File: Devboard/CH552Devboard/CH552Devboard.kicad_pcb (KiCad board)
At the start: 2 copper layers, 25.6 x 24.6 mm, 14 parts, among them J1 D+, J2 USB_B_Micro, J3 System, J4 GPIO, SW1 SW_Push, SW2 SW_Push, SW3 SW_Push, SW4 SW_Push, U1 CH552T

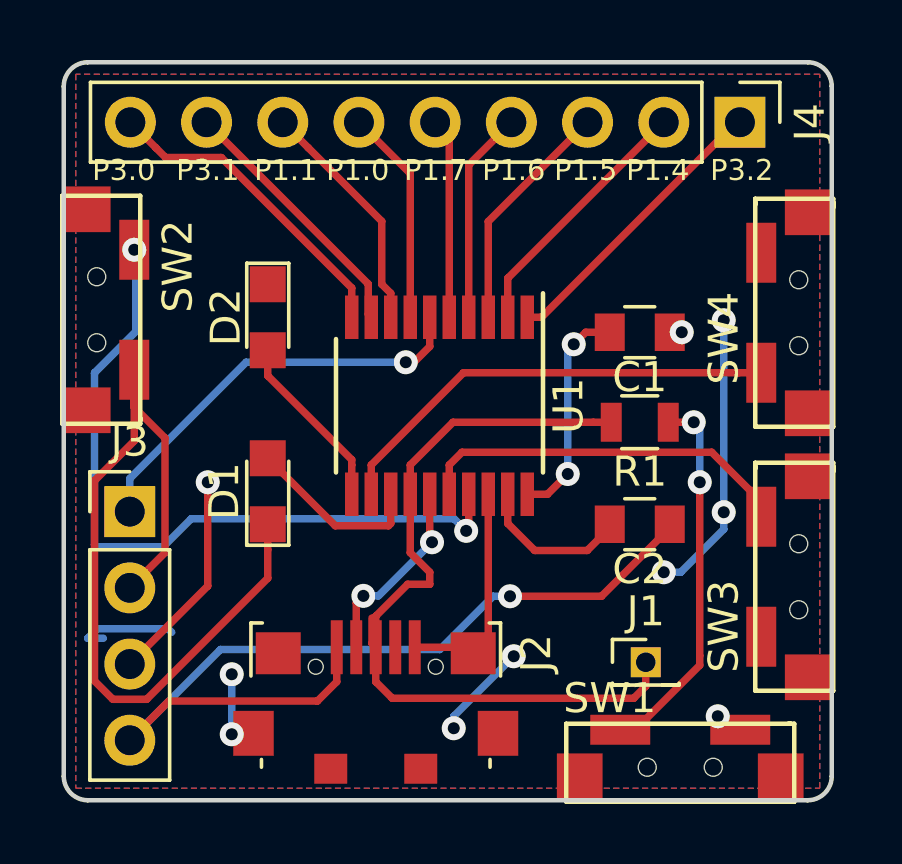
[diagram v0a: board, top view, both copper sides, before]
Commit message: Recieved V1, fixed issue. Seems to work now.
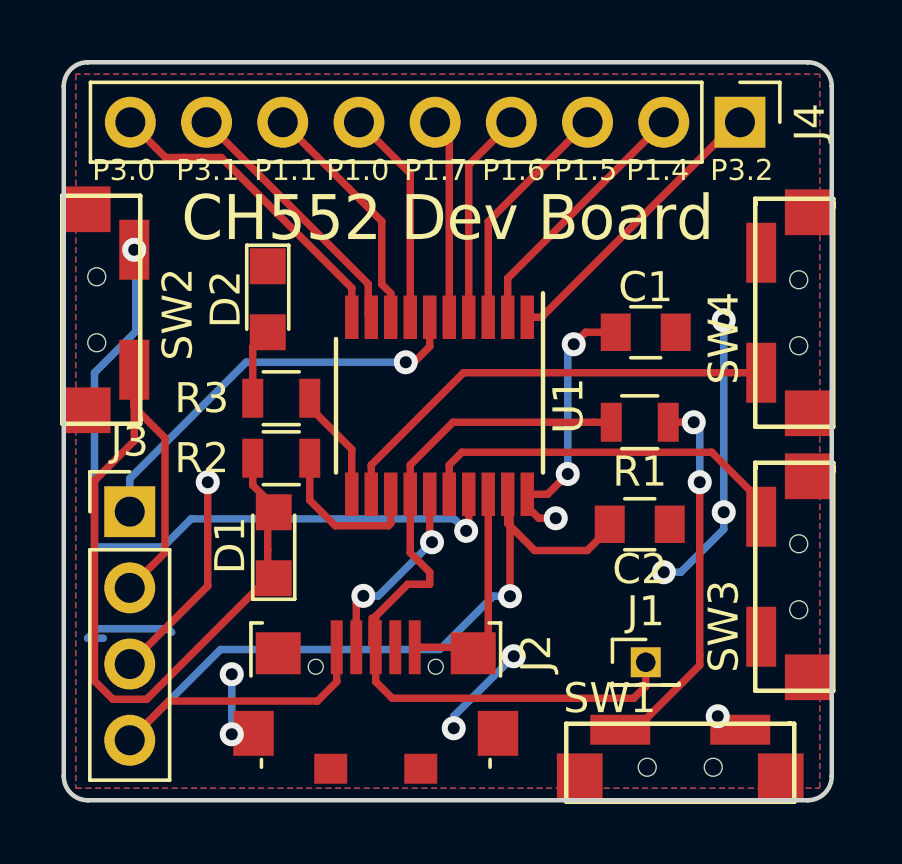
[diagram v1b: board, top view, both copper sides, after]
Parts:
- added R2: 330ohm, Resistors_SMD:R_0805, F.Cu at (163.2, 111.2)
- added R3: 330ohm, Resistors_SMD:R_0805, F.Cu at (163.2, 109.2)
- C1, C2: value C_Small -> 0.1uF
- moved D1 1.81 mm to (163.0, 114.1)
- moved D2 0.60 mm to (162.8, 105.9)
- moved C1 0.20 mm to (175.4, 107.0), turned to 0 degrees
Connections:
- C1 pad 2: Net-(C1-Pad2) -> VSS
- C2 pad 1: VCC -> VSS
- C2 pad 2: Net-(C2-Pad2) -> VCC
- U1 pad 11: Net-(D2-Pad2) -> Net-(R3-Pad2)
- U1 pad 13: Net-(D1-Pad2) -> Net-(R2-Pad2)
- U1 pad 19: Net-(C2-Pad2) -> VCC
- U1 pad 20: Net-(C1-Pad2) -> +3V3
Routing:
- net +3V3: track 7.14 -> 15.6 mm, vias 3 -> 5
- net Net-(C1-Pad2): track 7.40 -> 0.00 mm, vias 2 -> 0
- net Net-(R2-Pad2): track 0.00 -> 5.46 mm
- net Net-(C2-Pad2): track 5.18 -> 0.00 mm
- net Net-(D1-Pad2): track 6.04 -> 2.08 mm
- net Net-(R3-Pad2): track 0.00 -> 3.78 mm
- net Net-(D2-Pad2): track 5.96 -> 2.41 mm
- net VCC: track 29.9 -> 32.1 mm
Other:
- board text added: "CH552 Dev Board"
- board text added: "V2"

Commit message: Added silkscreen to devboard
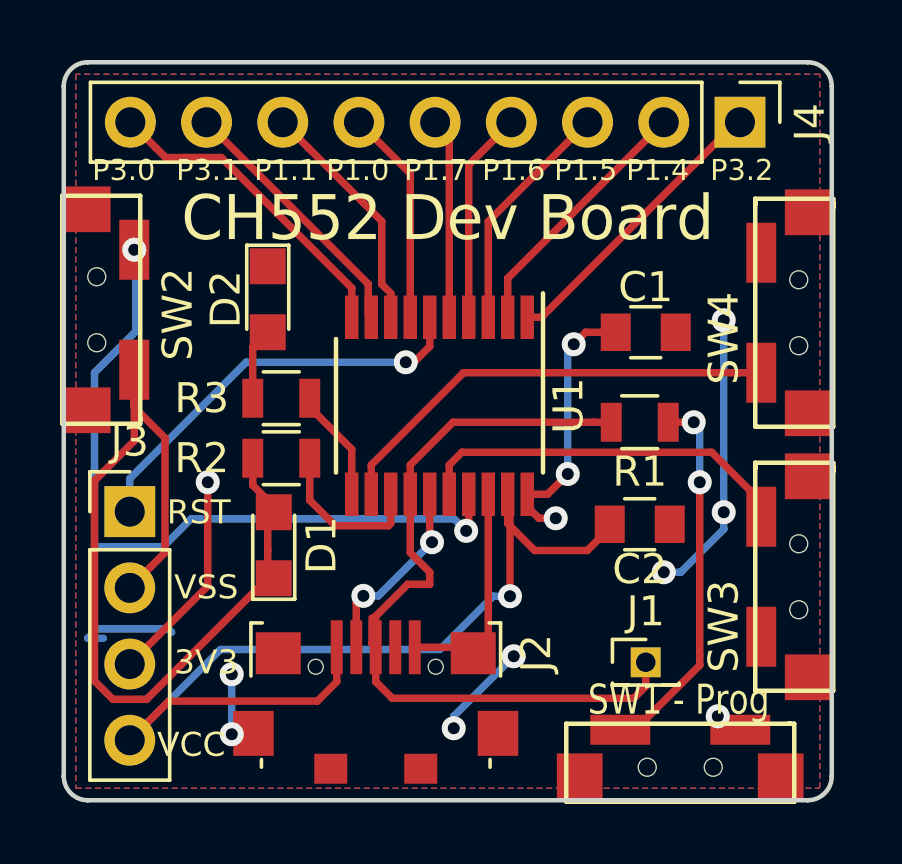
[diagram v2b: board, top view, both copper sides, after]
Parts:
- SW1 - Prog: renamed from SW1
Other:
- board text added: "3V3"
- board text added: "D1: P3.5 D2: P3.3 SW2: P1.2 SW3: P1.3 SW4: P3.4"
- board text added: "RST"
- board text added: "To Program: Reset uC while holding SW1 (Prog)"
- board text added: "VCC"
- board text added: "VSS"
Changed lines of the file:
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@@
   (general
     (thickness 1.6)
-    (drawings 19)
+    (drawings 25)
     (tracks 172)
     (zones 0)
@@
     (tags "LED led 0805 SMD smd SMT smt smdled SMDLED smtled SMTLED")
     (attr smd)
-    (fp_text reference D1 (at 0 -1.45 90) (layer F.SilkS)
+    (fp_text reference D1 (at 0 1.592 90) (layer F.SilkS)
       (effects (font (size 1 1) (thickness 0.15)))
     )
@@
   (module CH552:Ali_button (layer F.Cu)
     (at 176.7 121.65)
-    (fp_text reference SW1 (at -2.5 -2.45) (layer F.SilkS)
-      (effects (font (size 1 1) (thickness 0.15)))
+    (fp_text reference "SW1 - Prog" (at -0.2 -2.4) (layer F.SilkS)
+      (effects (font (size 1 0.8) (thickness 0.15)))
     )
     (fp_text value SW_Push (at -0.15 -3.15) (layer F.Fab)
@@
     )
   )
+  (gr_text "D1: P3.5\nD2: P3.3\nSW2: P1.2\nSW3: P1.3\nSW4: P3.4" (at 169.75 116) (layer B.SilkS)
+    (effects (font (size 1.5 1.5) (thickness 0.3)) (justify mirror))
+  )
+  (gr_text "To Program:\nReset uC while \nholding SW1 (Prog)" (at 168.75 105.5) (layer B.SilkS)
+    (effects (font (size 1.5 1.5) (thickness 0.3)) (justify mirror))
+  )
+  (gr_text VCC (at 160.25 120.75) (layer F.SilkS)
+    (effects (font (size 0.8 0.8) (thickness 0.2)))
+  )
+  (gr_text 3V3 (at 160.75 118) (layer F.SilkS)
+    (effects (font (size 0.8 0.8) (thickness 0.2)))
+  )
+  (gr_text VSS (at 160.75 115.5) (layer F.SilkS)
+    (effects (font (size 0.8 0.8) (thickness 0.2)))
+  )
+  (gr_text "RST\n" (at 160.5 113) (layer F.SilkS)
+    (effects (font (size 0.8 0.8) (thickness 0.2)))
+  )
   (gr_text "CH552 Dev Board\n" (at 168.8 103.2) (layer F.SilkS)
     (effects (font (size 1.5 1.45) (thickness 0.3)))
@@
   (segment (start 171.834315 113.2) (end 171.484325 112.85001) (width 0.25) (layer F.Cu) (net 1))
   (segment (start 172.4 113.2) (end 171.834315 113.2) (width 0.25) (layer F.Cu) (net 1))
-  (via (at 172.8 111.725) (size 0.8) (drill 0.4) (layers F.Cu B.Cu) (net 1) (status 1000000))
-  (segment (start 174 107) (end 174.2 107) (width 0.25) (layer F.Cu) (net 1) (status 1000000))
-  (segment (start 173.4 107) (end 174 107) (width 0.25) (layer F.Cu) (net 1) (status 1000000))
-  (segment (start 173 107.4) (end 173.4 107) (width 0.25) (layer F.Cu) (net 1) (status 1000000))
-  (segment (start 172.8 107.6) (end 173 107.4) (width 0.25) (layer B.Cu) (net 1) (status 1000000))
-  (segment (start 172.8 111.725) (end 172.8 107.6) (width 0.25) (layer B.Cu) (net 1) (status 1000000))
-  (via (at 173 107.4) (size 0.8) (drill 0.4) (layers F.Cu B.Cu) (net 1) (status 1000000))
-  (segment (start 172.125 112.4) (end 172.8 111.725) (width 0.25) (layer F.Cu) (net 1) (status 1000000))
-  (segment (start 171.45 112.4) (end 172.125 112.4) (width 0.25) (layer F.Cu) (net 1) (status 1000000))
+  (via (at 172.8 111.725) (size 0.8) (drill 0.4) (layers F.Cu B.Cu) (net 1))
+  (segment (start 174 107) (end 174.2 107) (width 0.25) (layer F.Cu) (net 1))
+  (segment (start 173.4 107) (end 174 107) (width 0.25) (layer F.Cu) (net 1))
+  (segment (start 173 107.4) (end 173.4 107) (width 0.25) (layer F.Cu) (net 1))
+  (segment (start 172.8 107.6) (end 173 107.4) (width 0.25) (layer B.Cu) (net 1))
+  (segment (start 172.8 111.725) (end 172.8 107.6) (width 0.25) (layer B.Cu) (net 1))
+  (via (at 173 107.4) (size 0.8) (drill 0.4) (layers F.Cu B.Cu) (net 1))
+  (segment (start 172.125 112.4) (end 172.8 111.725) (width 0.25) (layer F.Cu) (net 1))
+  (segment (start 171.45 112.4) (end 172.125 112.4) (width 0.25) (layer F.Cu) (net 1))
   (segment (start 174.2 113.525) (end 174.2 113.4) (width 0.25) (layer F.Cu) (net 2))
   (segment (start 171.7 114.275) (end 173.45 114.275) (width 0.25) (layer F.Cu) (net 2))
@@
   (segment (start 170.875 112.475) (end 170.8 112.4) (width 0.25) (layer F.Cu) (net 2))
   (segment (start 170.875 115.8) (end 170.875 112.475) (width 0.25) (layer F.Cu) (net 2))
-  (segment (start 176.2 113.4) (end 176.2 113.525) (width 0.25) (layer F.Cu) (net 4))
   (segment (start 163 112.96359) (end 163.018205 112.981795) (width 0.25) (layer F.Cu) (net 3))
   (segment (start 163 112.8) (end 163 112.96359) (width 0.25) (layer F.Cu) (net 3))
   (segment (start 162.3 112.1) (end 163 112.8) (width 0.25) (layer F.Cu) (net 3))
   (segment (start 162.3 111.2) (end 162.3 112.1) (width 0.25) (layer F.Cu) (net 3))
-  (segment (start 166.824999 113.450001) (end 166.9 113.375) (width 0.25) (layer F.Cu) (net 23))
-  (segment (start 165.050001 113.450001) (end 166.824999 113.450001) (width 0.25) (layer F.Cu) (net 23))
-  (segment (start 166.9 113.375) (end 166.9 112.4) (width 0.25) (layer F.Cu) (net 23))
+  (segment (start 176.2 113.4) (end 176.2 113.525) (width 0.25) (layer F.Cu) (net 4))
   (segment (start 170.15 117.2) (end 169.65 117.7) (width 0.25) (layer F.Cu) (net 4))
   (segment (start 170.15 112.4) (end 170.15 117.2) (width 0.25) (layer F.Cu) (net 4))
@@
   (segment (start 178.5 108.35) (end 179.25 108.35) (width 0.25) (layer F.Cu) (net 22))
   (segment (start 166.25 112.4) (end 166.25 111.425) (width 0.25) (layer F.Cu) (net 22))
+  (segment (start 166.824999 113.450001) (end 166.9 113.375) (width 0.25) (layer F.Cu) (net 23))
+  (segment (start 165.050001 113.450001) (end 166.824999 113.450001) (width 0.25) (layer F.Cu) (net 23))
+  (segment (start 166.9 113.375) (end 166.9 112.4) (width 0.25) (layer F.Cu) (net 23))
   (segment (start 164.2 112.6) (end 164.2 111.2) (width 0.25) (layer F.Cu) (net 23))
   (segment (start 165.050001 113.450001) (end 164.2 112.6) (width 0.25) (layer F.Cu) (net 23))
